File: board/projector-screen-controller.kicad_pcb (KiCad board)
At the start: 2 copper layers, 97.2 x 106 mm, 63 parts, among them J1 ICSP, J2 MSTBVA 2,5 HC/ 3-G, J3 MCV-3-G, J4 MCV-3-G, J5 MCV-3-G, J6 MSTBVA 2,5/ 6-G, J7 MCV-3-G, K1 JS1-12V-F, K2 JS1-12V-F, K3 JS1-12V-F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

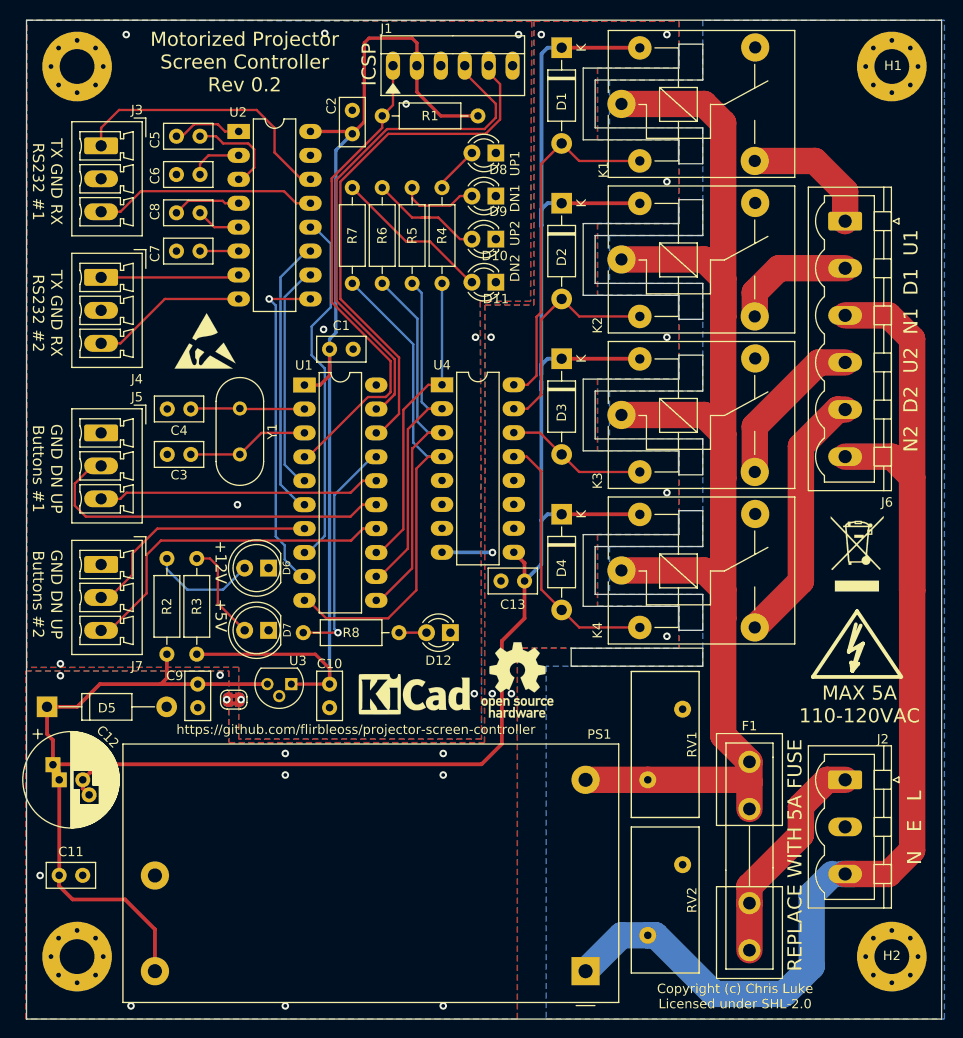
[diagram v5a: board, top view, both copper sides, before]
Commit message: Via tweaks; update earth flood
* Tweak some via locations.
* Update some of the earth flood fill around relay pins that was missed
  previously.
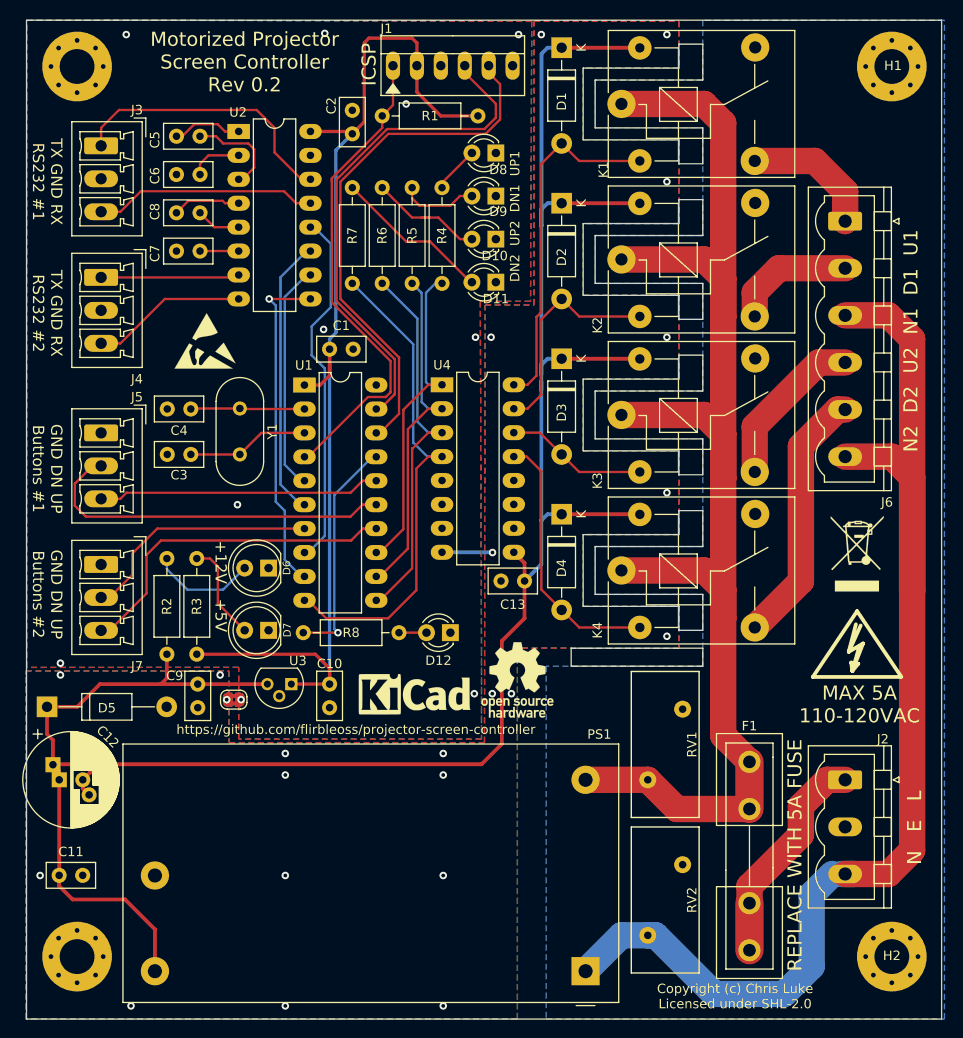
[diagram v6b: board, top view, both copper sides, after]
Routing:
- net /MCU/D1_UP_TTL: track 32.6 -> 35.2 mm
- net LINE: track 149.9 -> 151.1 mm
- net GNDPWR: vias 22 -> 24
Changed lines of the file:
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@@
     (thickness 1.6)
     (drawings 90)
-    (tracks 414)
+    (tracks 419)
     (zones 0)
     (modules 63)
@@
   (via (at 126.873 46.609) (size 0.8) (drill 0.4) (layers F.Cu B.Cu) (net 2))
   (via (at 122.174 116.586) (size 0.8) (drill 0.4) (layers F.Cu B.Cu) (net 2))
-  (via (at 78.232 113.411) (size 0.8) (drill 0.4) (layers F.Cu B.Cu) (net 2))
+  (via (at 78.232 113.35) (size 0.8) (drill 0.4) (layers F.Cu B.Cu) (net 2))
   (via (at 85.217 46.609) (size 0.8) (drill 0.4) (layers F.Cu B.Cu) (net 2))
   (via (at 106.299 46.482) (size 0.8) (drill 0.4) (layers F.Cu B.Cu) (net 2))
@@
   (segment (start 117.295 83.7946) (end 114.635039 86.454561) (width 0.25) (layer F.Cu) (net 12))
   (segment (start 118.745 83.7946) (end 117.295 83.7946) (width 0.25) (layer F.Cu) (net 12) (status 10))
-  (segment (start 118.745 83.7946) (end 118.745 73.025) (width 0.25) (layer B.Cu) (net 12) (status 30))
+  (segment (start 118.0465 73.025) (end 118.745 73.025) (width 0.25) (layer B.Cu) (net 12))
+  (segment (start 117.0432 74.0283) (end 118.0465 73.025) (width 0.25) (layer B.Cu) (net 12))
+  (segment (start 117.0432 83.5152) (end 117.0432 74.0283) (width 0.25) (layer B.Cu) (net 12))
+  (segment (start 118.745 83.7946) (end 117.3226 83.7946) (width 0.25) (layer B.Cu) (net 12))
+  (segment (start 117.3226 83.7946) (end 117.0432 83.5152) (width 0.25) (layer B.Cu) (net 12))
   (segment (start 115.119989 101.180011) (end 112.16 104.14) (width 0.25) (layer F.Cu) (net 13) (status 20))
   (segment (start 112.16 104.14) (end 111.76 104.14) (width 0.25) (layer F.Cu) (net 13) (status 30))
@@
   (segment (start 148.594999 121.035999) (end 151.384 123.825) (width 2.8) (layer F.Cu) (net 23) (status 20))
   (segment (start 148.594999 108.589999) (end 148.594999 121.035999) (width 2.8) (layer F.Cu) (net 23))
-  (segment (start 151.13 125.73) (end 151.384 125.984) (width 2.8) (layer F.Cu) (net 23))
-  (segment (start 140.589 125.73) (end 151.13 125.73) (width 2.8) (layer F.Cu) (net 23) (status 10))
-  (segment (start 151.384 123.825) (end 151.384 125.984) (width 2.8) (layer F.Cu) (net 23) (status 10))
-  (segment (start 151.384 125.984) (end 151.384 128.825) (width 2.8) (layer F.Cu) (net 23) (status 20))
+  (segment (start 151.384 123.825) (end 151.384 128.825) (width 3) (layer F.Cu) (net 23) (status 30))
   (segment (start 140.589 125.73) (end 133.985 125.73) (width 2.8) (layer F.Cu) (net 23) (status 30))
+  (segment (start 143.684 128.825) (end 140.589 125.73) (width 2.8) (layer F.Cu) (net 23) (status 20))
+  (segment (start 151.384 128.825) (end 143.684 128.825) (width 2.8) (layer F.Cu) (net 23) (status 10))
   (segment (start 141.4145 142.24) (end 140.589 142.24) (width 2.8) (layer B.Cu) (net 25) (status 30))
   (segment (start 157.988 137.922) (end 157.988 145.542) (width 2.8) (layer B.Cu) (net 25))
@@
   (segment (start 126.365 91.4146) (end 127.7366 91.4146) (width 0.25) (layer F.Cu) (net 33) (status 10))
   (segment (start 127.7366 91.4146) (end 129.286 92.964) (width 0.25) (layer F.Cu) (net 33))
-  (segment (start 151.384 138.825) (end 151.384 143.825) (width 2.8) (layer F.Cu) (net 34) (status 30))
+  (segment (start 151.384 138.825) (end 151.384 143.825) (width 3) (layer F.Cu) (net 34) (status 30))
   (segment (start 151.384 137.033) (end 151.384 138.825) (width 2.8) (layer F.Cu) (net 34) (status 20))
   (segment (start 156.845 131.572) (end 151.384 137.033) (width 2.8) (layer F.Cu) (net 34))
@@
   (segment (start 104.775 74.676) (end 100.3935 74.676) (width 0.25) (layer F.Cu) (net 38) (status 10))
   (segment (start 101.092 75.3745) (end 100.3935 74.676) (width 0.25) (layer B.Cu) (net 38))
-  (segment (start 101.092 99.8855) (end 101.092 75.3745) (width 0.25) (layer B.Cu) (net 38))
-  (segment (start 102.0445 100.838) (end 101.092 99.8855) (width 0.25) (layer B.Cu) (net 38))
-  (segment (start 102.0445 102.362) (end 102.0445 100.838) (width 0.25) (layer B.Cu) (net 38))
+  (segment (start 101.092 96.2025) (end 101.092 75.3745) (width 0.25) (layer B.Cu) (net 38))
+  (segment (start 102.0445 97.155) (end 101.092 96.2025) (width 0.25) (layer B.Cu) (net 38))
+  (segment (start 102.0445 102.362) (end 102.0445 97.155) (width 0.25) (layer B.Cu) (net 38))
   (segment (start 104.14 104.14) (end 103.8225 104.14) (width 0.25) (layer B.Cu) (net 38) (status 30))
   (segment (start 103.8225 104.14) (end 102.0445 102.362) (width 0.25) (layer B.Cu) (net 38) (status 10))
@@
   (via (at 123.952 78.74) (size 0.8) (drill 0.4) (layers F.Cu B.Cu) (net 59))
   (via (at 82.55 122.936) (size 0.8) (drill 0.4) (layers F.Cu B.Cu) (net 59))
-  (via (at 78.232 114.681) (size 0.8) (drill 0.4) (layers F.Cu B.Cu) (net 59))
+  (via (at 78.232 114.6) (size 0.8) (drill 0.4) (layers F.Cu B.Cu) (net 59))
   (via (at 76.073 135.89) (size 0.8) (drill 0.4) (layers F.Cu B.Cu) (net 59))
   (via (at 118.872 149.733) (size 0.8) (drill 0.4) (layers F.Cu B.Cu) (net 59))
@@
   (via (at 142.621 95.25) (size 0.8) (drill 0.4) (layers F.Cu B.Cu) (net 59))
   (via (at 142.621 110.49) (size 0.8) (drill 0.4) (layers F.Cu B.Cu) (net 59))
-  (via (at 95.1865 114.6175) (size 0.8) (drill 0.4) (layers F.Cu B.Cu) (net 59))
+  (via (at 95.1865 114.6) (size 0.8) (drill 0.4) (layers F.Cu B.Cu) (net 59))
+  (via (at 118.872 135.89) (size 0.8) (drill 0.4) (layers F.Cu B.Cu) (net 59))
+  (via (at 102.108 135.89) (size 0.8) (drill 0.4) (layers F.Cu B.Cu) (net 59))
   (zone (net 0) (net_name "") (layers F&B.Cu) (hatch edge 0.508)
     (connect_pads (clearance 0.508))
@@
     (polygon
       (pts
-        (xy 146.431 45.085) (xy 146.431 51.435) (xy 136.525 51.435) (xy 136.525 56.515) (xy 146.431 56.515)
-        (xy 146.431 67.945) (xy 136.525 67.945) (xy 136.525 73.025) (xy 146.431 73.025) (xy 146.431 84.455)
-        (xy 136.525 84.455) (xy 136.525 89.535) (xy 146.431 89.535) (xy 146.431 100.965) (xy 136.525 100.965)
-        (xy 136.525 106.045) (xy 146.431 106.045) (xy 146.431 113.665) (xy 129.794 113.665) (xy 129.794 151.13)
+        (xy 146.431 45.085) (xy 146.431 51.435) (xy 135.001 51.435) (xy 135.001 56.515) (xy 146.431 56.515)
+        (xy 146.431 67.945) (xy 135.001 67.945) (xy 135.001 73.025) (xy 146.431 73.025) (xy 146.431 84.455)
+        (xy 135.001 84.455) (xy 135.001 89.535) (xy 146.431 89.535) (xy 146.431 100.965) (xy 135.001 100.965)
+        (xy 135.001 106.045) (xy 146.431 106.045) (xy 146.431 113.665) (xy 129.794 113.665) (xy 129.794 151.13)
         (xy 162.56 151.13) (xy 172.085 151.13) (xy 172.085 139.7) (xy 172.085 53.34) (xy 172.085 45.085)
         (xy 162.56 45.085)
@@
       (pts
         (xy 74.549 114.173) (xy 96.139 114.173) (xy 96.139 121.793) (xy 123.2535 121.793) (xy 123.317 75.311)
-        (xy 128.524 75.311) (xy 128.524 45.212) (xy 143.891 45.212) (xy 143.891 50.165) (xy 135.255 50.165)
-        (xy 135.255 57.785) (xy 143.891 57.785) (xy 143.891 66.675) (xy 135.255 66.675) (xy 135.255 74.295)
-        (xy 143.891 74.295) (xy 143.891 83.185) (xy 135.255 83.185) (xy 135.255 90.805) (xy 143.891 90.805)
-        (xy 143.891 99.695) (xy 135.255 99.695) (xy 135.255 107.315) (xy 143.891 107.315) (xy 143.891 111.76)
+        (xy 128.524 75.311) (xy 128.524 45.212) (xy 143.891 45.212) (xy 143.891 50.165) (xy 133.731 50.165)
+        (xy 133.731 57.785) (xy 143.891 57.785) (xy 143.891 66.675) (xy 133.731 66.675) (xy 133.731 74.295)
+        (xy 143.891 74.295) (xy 143.891 83.185) (xy 133.731 83.185) (xy 133.731 90.805) (xy 143.891 90.805)
+        (xy 143.891 99.695) (xy 133.731 99.695) (xy 133.731 107.315) (xy 143.891 107.315) (xy 143.891 111.76)
         (xy 133.985 111.76) (xy 126.746 111.76) (xy 126.746 151.13) (xy 74.549 151.13) (xy 74.549 114.554)
       )
@@
       (pts
         (xy 74.549 114.173) (xy 96.139 114.173) (xy 96.139 121.773214) (xy 123.2535 121.773214) (xy 123.317 75.311)
-        (xy 128.524 75.311) (xy 128.524 45.192214) (xy 143.891 45.192214) (xy 143.891 50.145214) (xy 135.255 50.145214)
-        (xy 135.255 57.765214) (xy 143.891 57.785) (xy 143.891 66.675) (xy 135.255 66.655214) (xy 135.255 74.275214)
-        (xy 143.891 74.295) (xy 143.891 83.185) (xy 135.255 83.165214) (xy 135.255 90.785214) (xy 143.891 90.805)
-        (xy 143.891 99.695) (xy 135.255 99.675214) (xy 135.255 107.295214) (xy 143.891 107.315) (xy 143.891 111.76)
+        (xy 128.524 75.311) (xy 128.524 45.192214) (xy 143.891 45.192214) (xy 143.891 50.145214) (xy 133.731 50.165)
+        (xy 133.731 57.785) (xy 143.891 57.785) (xy 143.891 66.675) (xy 133.731 66.675) (xy 133.731 74.295)
+        (xy 143.891 74.295) (xy 143.891 83.185) (xy 133.731 83.185) (xy 133.731 90.805) (xy 143.891 90.805)
+        (xy 143.891 99.695) (xy 133.731 99.695) (xy 133.731 107.315) (xy 143.891 107.315) (xy 143.891 111.76)
         (xy 133.985 111.740214) (xy 126.746 111.740214) (xy 126.746 151.110214) (xy 74.549 151.110214) (xy 74.549 114.534214)
       )

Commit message: Update xtal load capacitors, fix left mounting holes
* Try some 33pF caps for the crystal.
* Reflect the left side mounting holes in the schematic.
* Reroute one RS232 TTL line; though now more stuff runs under the clock
  lines so may move all the RS232 TTL traces later.
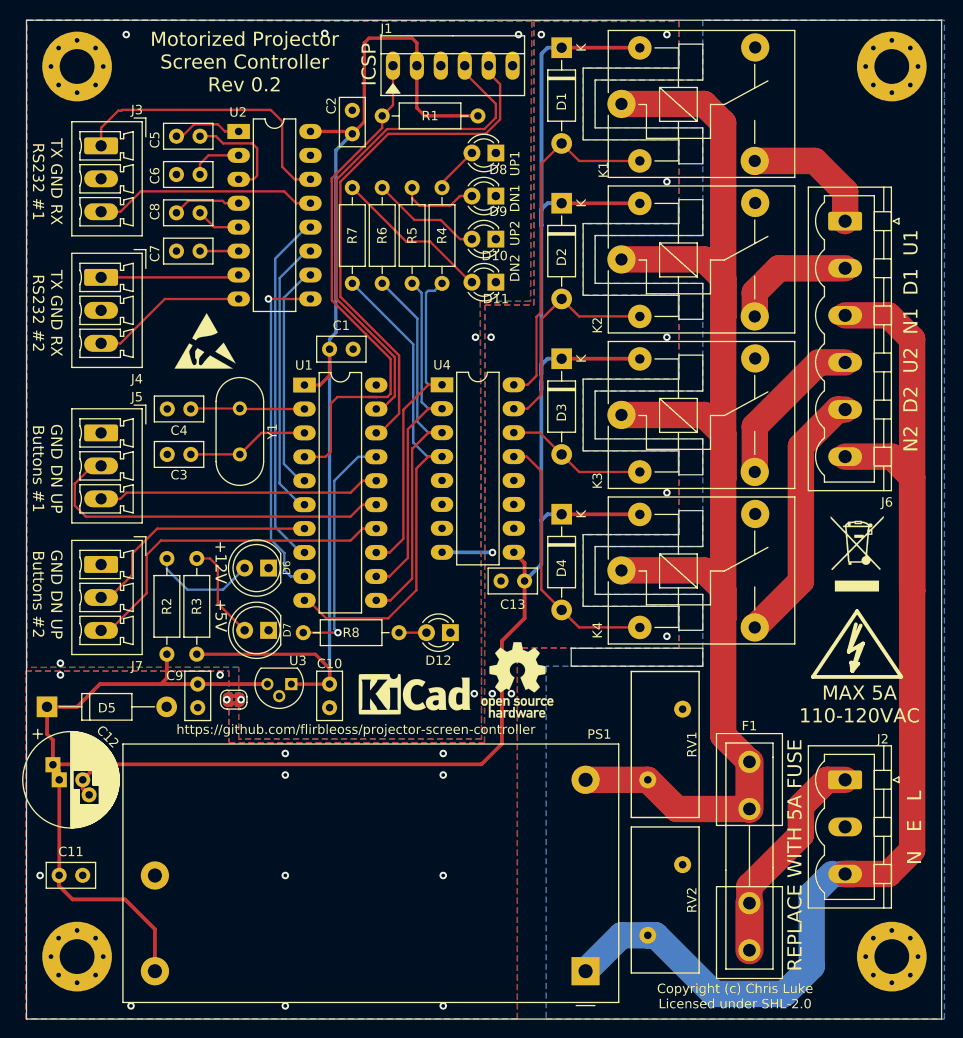
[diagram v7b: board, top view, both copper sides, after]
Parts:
- removed the REF** at (80.0, 50.0)
- removed the REF** at (80.0, 144.5)
- added H3: MountingHole_Pad, Mounting_Holes:MountingHole_3.7mm_Pad_Via, F.Cu at (80.0, 50.0)
- added H4: MountingHole_Pad, Mounting_Holes:MountingHole_3.7mm_Pad_Via, F.Cu at (80.0, 144.5)
- C3: value 20pF -> 330pF
- C4: value 20pF -> 33pF
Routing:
- net Net-(J1-Pad1): track 52.3 -> 56.7 mm
- net Net-(J1-Pad4): track 56.8 -> 54.7 mm
- net /MCU/TX1: track 29.5 -> 30.8 mm
- net Net-(C5-Pad2): track 10.4 -> 11.6 mm
- net +5V: track 119.7 -> 120.7 mm
- net Net-(D10-Pad2): track 12.7 -> 11.8 mm
- net Net-(R8-Pad1): track 24.6 -> 25.5 mm
- net Net-(U1-Pad8): track 38.6 -> 37.8 mm
- net /MCU/D2_UP_TTL: track 41.2 -> 41.8 mm
- net /MCU/D1_UP_TTL: track 35.2 -> 35.8 mm
- net Net-(U1-Pad9): track 36.2 -> 36.8 mm
- net /MCU/D1_DN_TTL: track 37.3 -> 37.8 mm
- net GND: vias 10 -> 7

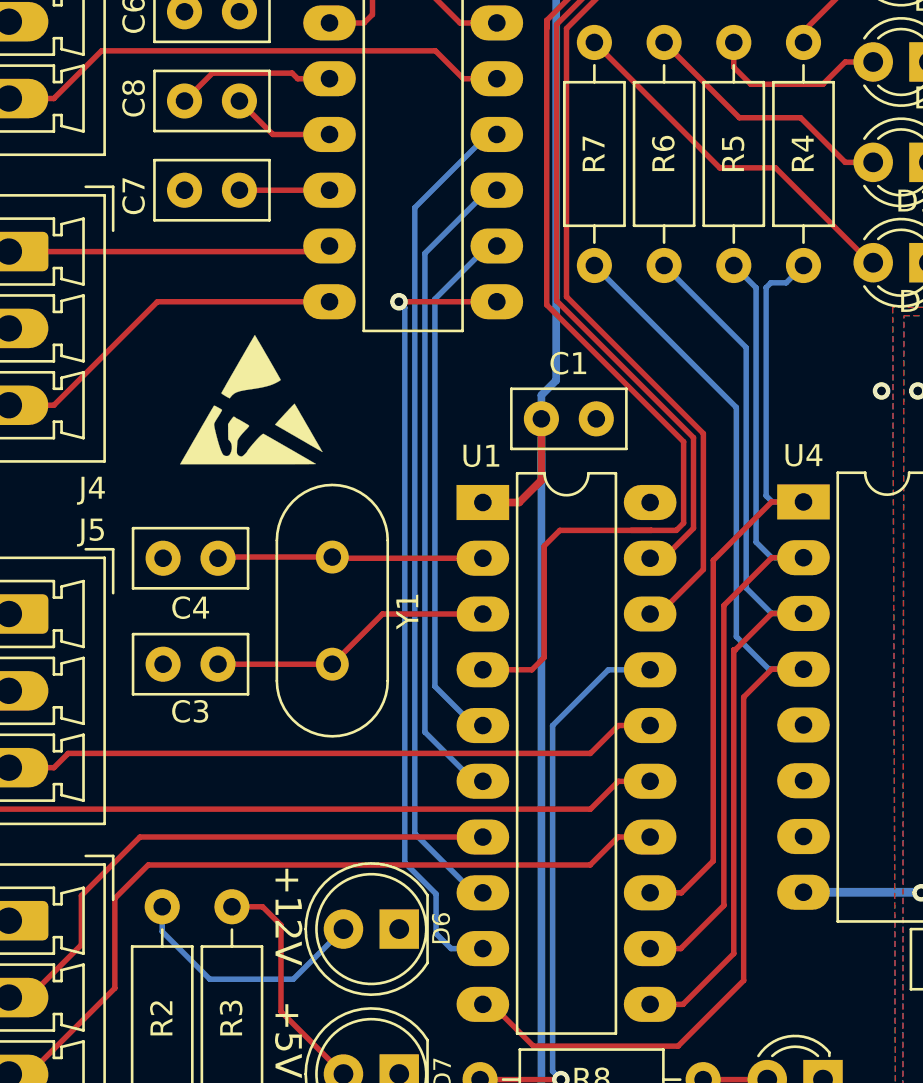
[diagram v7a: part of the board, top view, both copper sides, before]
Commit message: Make room for input filtering
* Move the crystal block up and isolate its ground plane.
* Route the RS232 TTL signals around the crystal block.
* Update images, PDFs and gerbers.
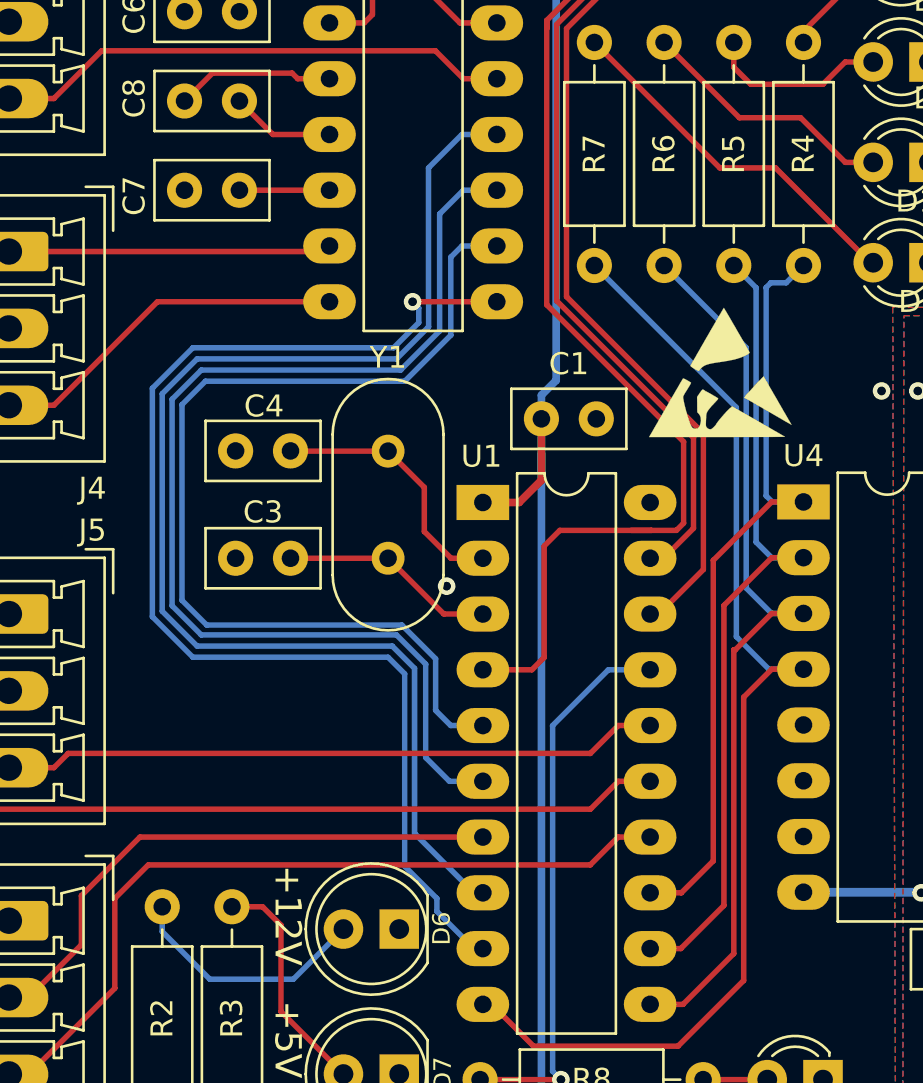
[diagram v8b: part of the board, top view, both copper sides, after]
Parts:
- C3: value 330pF -> 33pF
- moved REF*** 21.4 mm to (115.0, 77.9)
- moved C4 5.90 mm to (95.4, 81.5)
- moved C3 5.85 mm to (95.4, 86.4)
- moved Y1 5.45 mm to (99.8, 86.4)
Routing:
- net Net-(U1-Pad5): track 24.7 -> 46.1 mm
- net Net-(U1-Pad6): track 29.8 -> 51.2 mm
- net Net-(U1-Pad8): track 37.8 -> 58.6 mm
- net Net-(U1-Pad9): track 36.8 -> 55.5 mm
- net Net-(C3-Pad1): track 13.0 -> 9.82 mm
- net GND: vias 7 -> 8
